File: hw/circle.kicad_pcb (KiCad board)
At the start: 2 copper layers, 46 x 46 mm, 50 parts, among them J1 CONN_01X02, J2 USB_OTG, J3 CONN_01X03, J4 CONN_02X05, J5 CONN_01X03, J6 CONN_01X06, U1 STM32F303CCTx, U2 AS5048A, U3 DRV8312, U4 INA240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

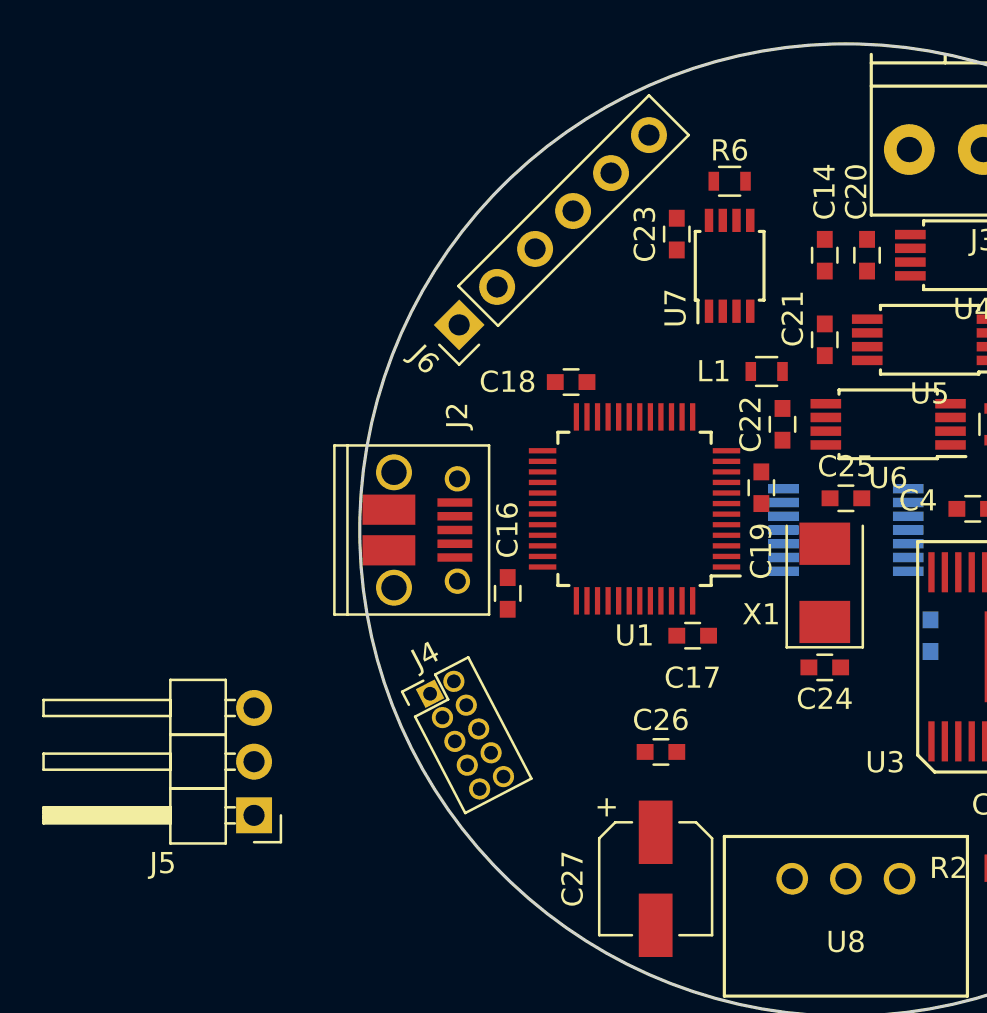
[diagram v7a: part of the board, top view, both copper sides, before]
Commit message: assign mcu pins
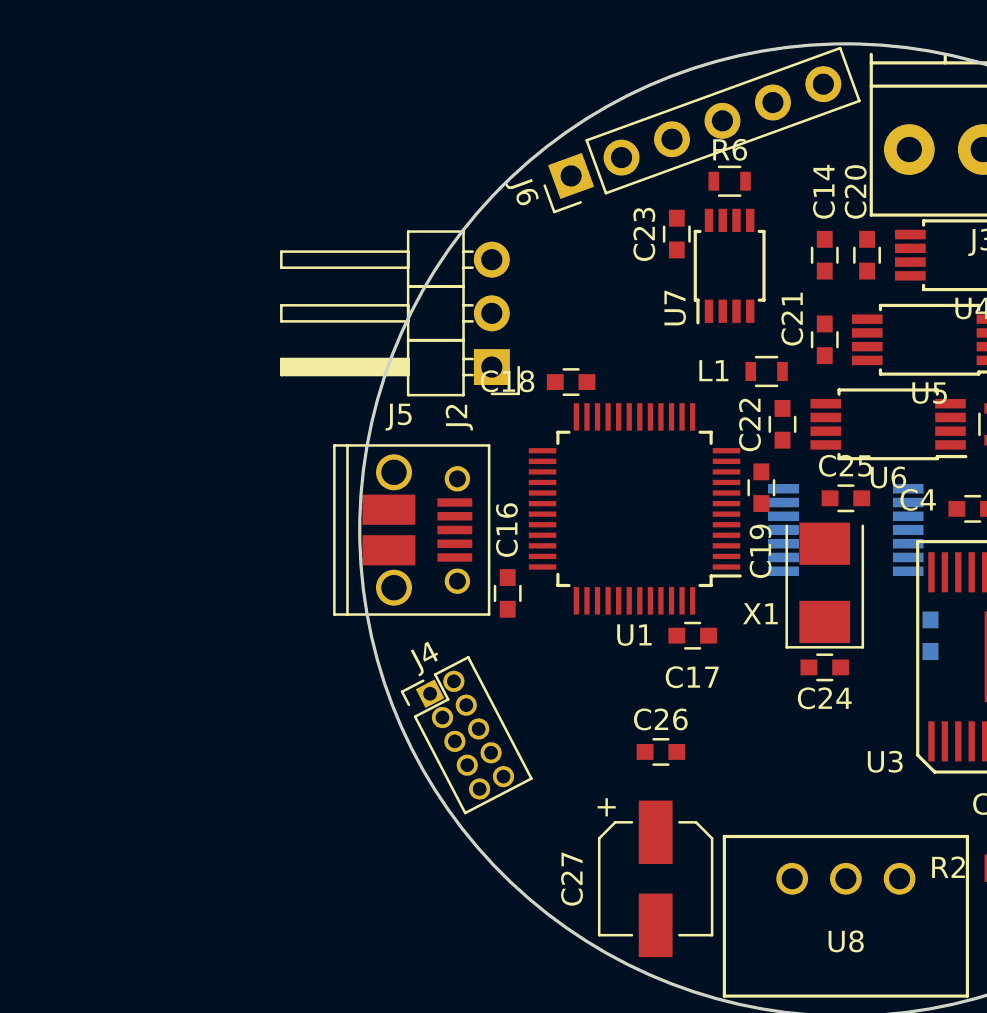
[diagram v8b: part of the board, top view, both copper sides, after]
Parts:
- moved J5 24.0 mm to (83.2, 92.3)
- moved J6 8.81 mm to (87.0, 83.2), turned to 110 degrees
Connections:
- U1 pad 10: Net-(U1-Pad10) -> /AMPC
- U1 pad 14: Net-(U1-Pad14) -> /AMPB
- U1 pad 15: Net-(U1-Pad15) -> /ENC_SCLK
- U1 pad 16: Net-(U1-Pad16) -> /ENC_MISO
- U1 pad 17: Net-(U1-Pad17) -> /ENC_MOSI
- U1 pad 18: Net-(U1-Pad18) -> /AMPA
- U1 pad 19: Net-(U1-Pad19) -> /RS485RE
- U1 pad 2: Net-(U1-Pad2) -> /FAULT
- U1 pad 20: Net-(U1-Pad20) -> /RS485DE
- U1 pad 21: Net-(U1-Pad21) -> /RS485DI
- U1 pad 22: Net-(U1-Pad22) -> /RS485RO
- U1 pad 30: Net-(U1-Pad30) -> /STDOUT
- U1 pad 31: Net-(U1-Pad31) -> /STDIN
- U1 pad 38: Net-(U1-Pad38) -> /ENC_CS
- U1 pad 39: Net-(U1-Pad39) -> /RSTA
- U1 pad 40: Net-(U1-Pad40) -> /RSTB
- U1 pad 41: Net-(U1-Pad41) -> /RSTC
- U1 pad 42: Net-(U1-Pad42) -> /PWMA
- U1 pad 43: Net-(U1-Pad43) -> /OTW
- U1 pad 45: Net-(U1-Pad45) -> /PWMB
- U1 pad 46: Net-(U1-Pad46) -> /PWMC
